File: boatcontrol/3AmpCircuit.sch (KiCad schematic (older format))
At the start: 5 parts, among them K901 G5RL-K1A-E-DC12, Q901 T9-818 3A, SW901 ESB30, SW902 ESB30

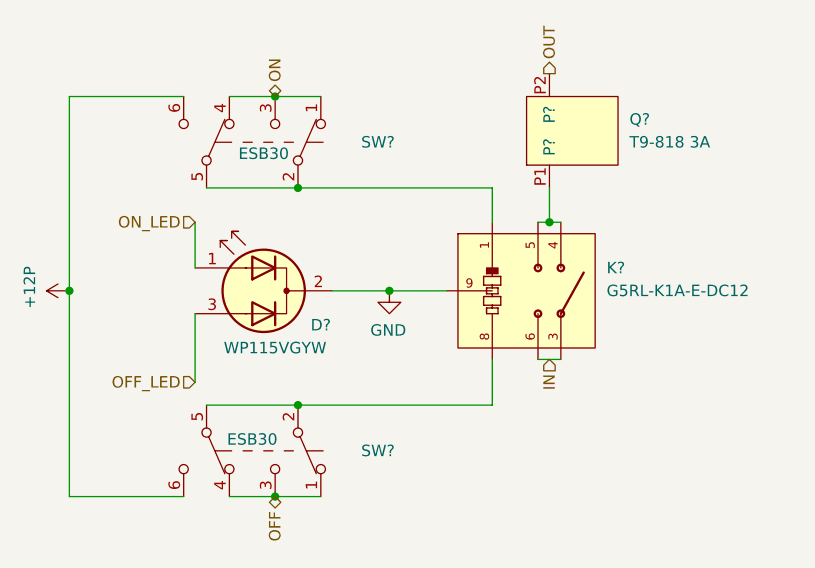
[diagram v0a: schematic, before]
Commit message: Change inductors
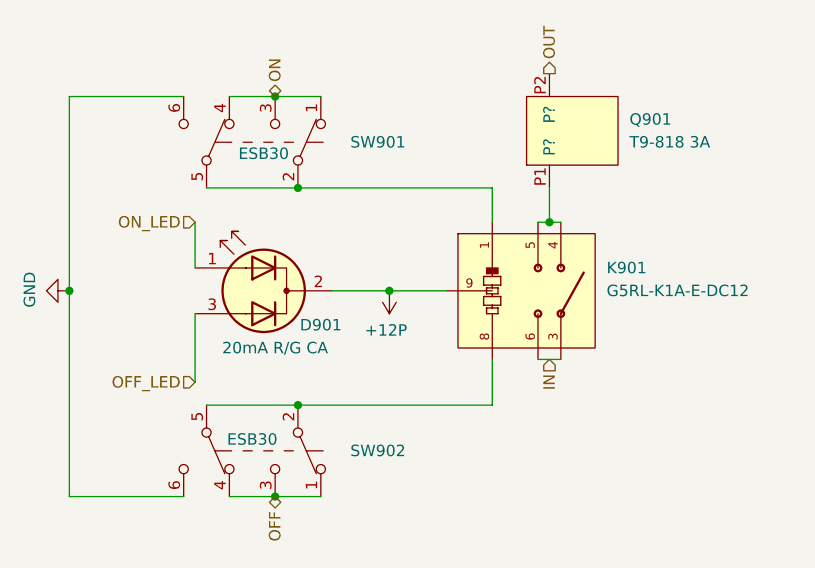
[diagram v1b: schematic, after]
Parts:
- D901: value WP115VGYW -> 20mA R/G CA; Manufacturer (none) -> Kingbright; Model (none) -> WP59EGW/CA
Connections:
- net +12P: now also D901.2 (K), K901.9 (C9); no longer SW901.6 (C), SW902.6 (C)
- net GND: now also SW901.6 (C), SW902.6 (C); no longer D901.2 (K), K901.9 (C9)
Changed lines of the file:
@@
 $Descr A4 11693 8268
 encoding utf-8
-Sheet 12 87
+Sheet 11 87
 Title "Boat Control Hat"
 Date "2020-07-09"
@@
 AR Path="/D1BB8DB4/5F75E923/60474907/6283485A" Ref="Q?"  Part="1"
 AR Path="/D1BB8DB4/5F75E923/60474911/6283485A" Ref="Q?"  Part="1"
-F 0 "Q?" V 7200 2750 50  0000 R CNN
+F 0 "Q901" V 7200 2750 50  0000 R CNN
 F 1 "T9-818 3A" V 7100 2750 50  0000 R CNN
 F 2 "BoatControl:Schurter_Circuit_Breaker" H 7150 3300 50  0001 C CNN
@@
 AR Path="/D1BB8DB4/5F75E923/60474907/63E25899" Ref="SW?"  Part="1"
 AR Path="/D1BB8DB4/5F75E923/60474911/63E25899" Ref="SW?"  Part="1"
-F 0 "SW?" V 6050 3900 50  0000 C CNN
+F 0 "SW901" V 6050 3900 50  0000 C CNN
 F 1 " ESB30" V 6000 3400 50  0000 C CNN
 F 2 "BoatControl:SW_PUSH_ESB30_DPDT" H 6050 3550 50  0001 C CNN
@@
 L power:GND #PWR?
 U 1 1 63ED7D79
-P 6650 4000
+P 5250 4000
 AR Path="/5FBFBEC9/63ED7D79" Ref="#PWR?"  Part="1"
 AR Path="/768425E1/63ED7D79" Ref="#PWR?"  Part="1"
@@
 AR Path="/D1BB8DB4/5F75E923/60474907/63ED7D79" Ref="#PWR?"  Part="1"
 AR Path="/D1BB8DB4/5F75E923/60474911/63ED7D79" Ref="#PWR?"  Part="1"
-F 0 "#PWR?" H 6650 3750 50  0001 C CNN
-F 1 "GND" H 6655 3827 50  0000 C CNN
-F 2 "" H 6650 4000 50  0001 C CNN
-F 3 "" H 6650 4000 50  0001 C CNN
-	1    6650 4000
-	-1   0    0    -1
+F 0 "#PWR0902" H 5250 3750 50  0001 C CNN
+F 1 "GND" H 5255 3827 50  0000 C CNN
+F 2 "" H 5250 4000 50  0001 C CNN
+F 3 "" H 5250 4000 50  0001 C CNN
+	1    5250 4000
+	0    1    -1   0
 $EndComp
 $Comp
 L power:+12P #PWR?
 U 1 1 D2B5CDA0
-P 5250 4000
+P 6650 4000
 AR Path="/5FBFBEC9/D2B5CDA0" Ref="#PWR?"  Part="1"
 AR Path="/768425E1/D2B5CDA0" Ref="#PWR?"  Part="1"
@@
 AR Path="/D1BB8DB4/5F75E923/60474907/D2B5CDA0" Ref="#PWR?"  Part="1"
 AR Path="/D1BB8DB4/5F75E923/60474911/D2B5CDA0" Ref="#PWR?"  Part="1"
-F 0 "#PWR?" H 5250 3850 50  0001 C CNN
-F 1 "+12P" H 5265 4173 50  0000 C CNN
-F 2 "" H 5250 4000 50  0001 C CNN
-F 3 "" H 5250 4000 50  0001 C CNN
-	1    5250 4000
-	0    -1   -1   0
+F 0 "#PWR0901" H 6650 3850 50  0001 C CNN
+F 1 "+12P" H 6665 4173 50  0000 C CNN
+F 2 "" H 6650 4000 50  0001 C CNN
+F 3 "" H 6650 4000 50  0001 C CNN
+	1    6650 4000
+	-1   0    0    1
 $EndComp
 $Comp
@@
 AR Path="/D1BB8DB4/5F75E923/60474907/D2B5CD9C" Ref="SW?"  Part="1"
 AR Path="/D1BB8DB4/5F75E923/60474911/D2B5CD9C" Ref="SW?"  Part="1"
-F 0 "SW?" V 6050 5250 50  0000 C CNN
+F 0 "SW902" V 6050 5250 50  0000 C CNN
 F 1 " ESB30" V 6000 4700 50  0000 C CNN
 F 2 "BoatControl:SW_PUSH_ESB30_DPDT" H 6050 4900 50  0001 C CNN
@@
 AR Path="/D1BB8DB4/5F75E923/60474907/E14E2027" Ref="D?"  Part="1"
 AR Path="/D1BB8DB4/5F75E923/60474911/E14E2027" Ref="D?"  Part="1"
-F 0 "D?" H 5850 3850 50  0000 C CNN
-F 1 "WP115VGYW" H 6050 3750 50  0000 C CNN
+F 0 "D901" H 5850 3850 50  0000 C CNN
+F 1 "20mA R/G CA" H 6050 3750 50  0000 C CNN
 F 2 "LED_THT:LED_D5.0mm-3" H 6100 4000 50  0001 C CNN
-F 3 "https://www.mouser.ca/datasheet/2/216/WP115VGYW-232005.pdf" H 6100 4000 50  0001 C CNN
+F 3 "http://www.kingbrightusa.com/images/catalog/SPEC/WP59EGW-CA.pdf" H 6100 4000 50  0001 C CNN
+F 4 "WP59EGW/CA" H 6100 4000 50  0001 C CNN "Model"
+F 5 "Kingbright" H 6100 4000 50  0001 C CNN "Manufacturer"
 	1    6100 4000
 	-1   0    0    -1
@@
 AR Path="/D1BB8DB4/5F75E923/60474907/D2F4D9A8" Ref="K?"  Part="1"
 AR Path="/D1BB8DB4/5F75E923/60474911/D2F4D9A8" Ref="K?"  Part="1"
-F 0 "K?" H 7600 4100 50  0000 L CNN
+F 0 "K901" H 7600 4100 50  0000 L CNN
 F 1 "G5RL-K1A-E-DC12" H 7600 4000 50  0000 L CNN
 F 2 "RELAY_G5RL-K1A-E-DC12" H 7600 4150 50  0001 L BNN

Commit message: CRC ErrorFree
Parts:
- renumbered D901 to D1101, K901 to K1101, Q901 to Q1101, SW901 to SW1101, SW902 to SW1102

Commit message: Resistance is futile
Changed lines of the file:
@@
 $Descr A4 11693 8268
 encoding utf-8
-Sheet 36 87
+Sheet 11 87
 Title "Boat Control Hat"
 Date "2020-07-09"
@@
 AR Path="/D1BB8DB4/5F75E923/60474907/6283485A" Ref="Q?"  Part="1"
 AR Path="/D1BB8DB4/5F75E923/60474911/6283485A" Ref="Q?"  Part="1"
-F 0 "Q3801" V 7200 2750 50  0000 R CNN
+F 0 "Q1101" V 7200 2750 50  0000 R CNN
 F 1 "T9-818 3A" V 7100 2750 50  0000 R CNN
 F 2 "BoatControl:Schurter_Circuit_Breaker" H 7150 3300 50  0001 C CNN
@@
 AR Path="/D1BB8DB4/5F75E923/60474907/63E25899" Ref="SW?"  Part="1"
 AR Path="/D1BB8DB4/5F75E923/60474911/63E25899" Ref="SW?"  Part="1"
-F 0 "SW3801" V 6050 3900 50  0000 C CNN
+F 0 "SW1101" V 6050 3900 50  0000 C CNN
 F 1 " ESB30" V 6000 3400 50  0000 C CNN
 F 2 "BoatControl:SW_PUSH_ESB30_DPDT" H 6050 3550 50  0001 C CNN
@@
 AR Path="/D1BB8DB4/5F75E923/60474907/D2B5CD9C" Ref="SW?"  Part="1"
 AR Path="/D1BB8DB4/5F75E923/60474911/D2B5CD9C" Ref="SW?"  Part="1"
-F 0 "SW3802" V 6050 5250 50  0000 C CNN
+F 0 "SW1102" V 6050 5250 50  0000 C CNN
 F 1 " ESB30" V 6000 4700 50  0000 C CNN
 F 2 "BoatControl:SW_PUSH_ESB30_DPDT" H 6050 4900 50  0001 C CNN
@@
 AR Path="/D1BB8DB4/5F75E923/60474907/E14E2027" Ref="D?"  Part="1"
 AR Path="/D1BB8DB4/5F75E923/60474911/E14E2027" Ref="D?"  Part="1"
-F 0 "D3801" H 5850 3850 50  0000 C CNN
+F 0 "D1101" H 5850 3850 50  0000 C CNN
 F 1 "20mA R/G CA" H 6050 3750 50  0000 C CNN
 F 2 "LED_THT:LED_D5.0mm-3" H 6100 4000 50  0001 C CNN
@@
 AR Path="/D1BB8DB4/5F75E923/60474907/D2F4D9A8" Ref="K?"  Part="1"
 AR Path="/D1BB8DB4/5F75E923/60474911/D2F4D9A8" Ref="K?"  Part="1"
-F 0 "K3801" H 7600 4100 50  0000 L CNN
+F 0 "K1101" H 7600 4100 50  0000 L CNN
 F 1 "G5RL-K1A-E-DC12" H 7600 4000 50  0000 L CNN
 F 2 "RELAY_G5RL-K1A-E-DC12" H 7600 4150 50  0001 L BNN

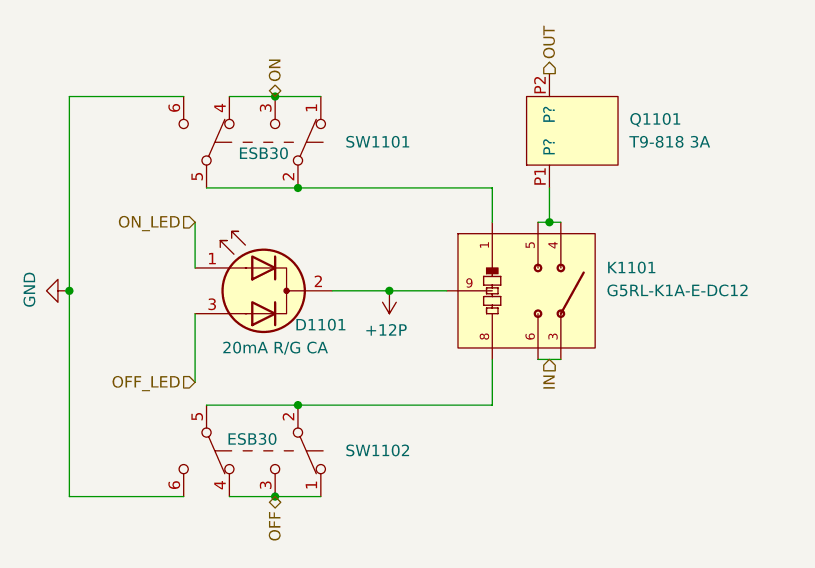
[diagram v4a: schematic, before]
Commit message: Remove resistor on protection, change MOSFET
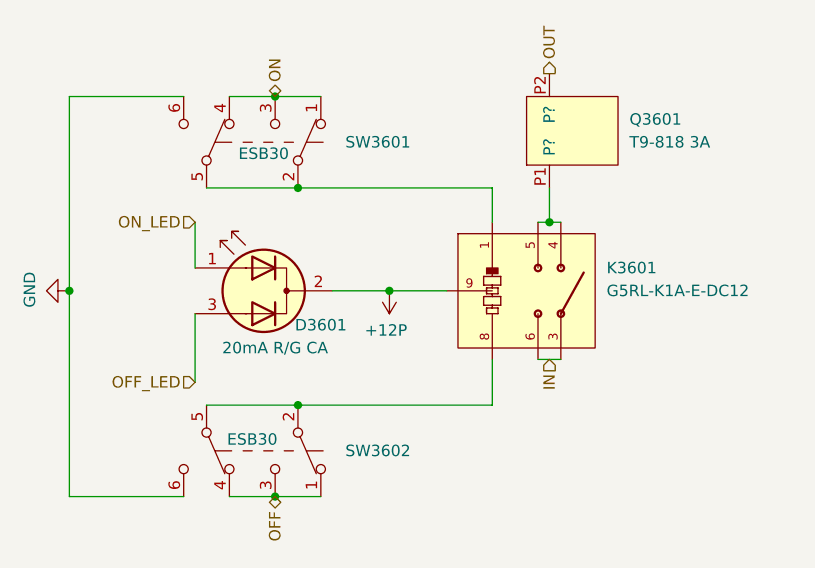
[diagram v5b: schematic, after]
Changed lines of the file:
@@
 $Descr A4 11693 8268
 encoding utf-8
-Sheet 11 87
+Sheet 36 87
 Title "Boat Control Hat"
 Date "2020-07-09"
@@
 AR Path="/D1BB8DB4/5F75E923/60474907/6283485A" Ref="Q?"  Part="1"
 AR Path="/D1BB8DB4/5F75E923/60474911/6283485A" Ref="Q?"  Part="1"
-F 0 "Q1101" V 7200 2750 50  0000 R CNN
+F 0 "Q3601" V 7200 2750 50  0000 R CNN
 F 1 "T9-818 3A" V 7100 2750 50  0000 R CNN
 F 2 "BoatControl:Schurter_Circuit_Breaker" H 7150 3300 50  0001 C CNN
@@
 AR Path="/D1BB8DB4/5F75E923/60474907/63E25899" Ref="SW?"  Part="1"
 AR Path="/D1BB8DB4/5F75E923/60474911/63E25899" Ref="SW?"  Part="1"
-F 0 "SW1101" V 6050 3900 50  0000 C CNN
+F 0 "SW3601" V 6050 3900 50  0000 C CNN
 F 1 " ESB30" V 6000 3400 50  0000 C CNN
 F 2 "BoatControl:SW_PUSH_ESB30_DPDT" H 6050 3550 50  0001 C CNN
@@
 AR Path="/D1BB8DB4/5F75E923/60474907/63ED7D79" Ref="#PWR?"  Part="1"
 AR Path="/D1BB8DB4/5F75E923/60474911/63ED7D79" Ref="#PWR?"  Part="1"
-F 0 "#PWR03801" H 5250 3750 50  0001 C CNN
+F 0 "#PWR03601" H 5250 3750 50  0001 C CNN
 F 1 "GND" H 5255 3827 50  0000 C CNN
 F 2 "" H 5250 4000 50  0001 C CNN
@@
 AR Path="/D1BB8DB4/5F75E923/60474907/D2B5CDA0" Ref="#PWR?"  Part="1"
 AR Path="/D1BB8DB4/5F75E923/60474911/D2B5CDA0" Ref="#PWR?"  Part="1"
-F 0 "#PWR03802" H 6650 3850 50  0001 C CNN
+F 0 "#PWR03602" H 6650 3850 50  0001 C CNN
 F 1 "+12P" H 6665 4173 50  0000 C CNN
 F 2 "" H 6650 4000 50  0001 C CNN
@@
 AR Path="/D1BB8DB4/5F75E923/60474907/D2B5CD9C" Ref="SW?"  Part="1"
 AR Path="/D1BB8DB4/5F75E923/60474911/D2B5CD9C" Ref="SW?"  Part="1"
-F 0 "SW1102" V 6050 5250 50  0000 C CNN
+F 0 "SW3602" V 6050 5250 50  0000 C CNN
 F 1 " ESB30" V 6000 4700 50  0000 C CNN
 F 2 "BoatControl:SW_PUSH_ESB30_DPDT" H 6050 4900 50  0001 C CNN
@@
 AR Path="/D1BB8DB4/5F75E923/60474907/E14E2027" Ref="D?"  Part="1"
 AR Path="/D1BB8DB4/5F75E923/60474911/E14E2027" Ref="D?"  Part="1"
-F 0 "D1101" H 5850 3850 50  0000 C CNN
+F 0 "D3601" H 5850 3850 50  0000 C CNN
 F 1 "20mA R/G CA" H 6050 3750 50  0000 C CNN
 F 2 "LED_THT:LED_D5.0mm-3" H 6100 4000 50  0001 C CNN
@@
 AR Path="/D1BB8DB4/5F75E923/60474907/D2F4D9A8" Ref="K?"  Part="1"
 AR Path="/D1BB8DB4/5F75E923/60474911/D2F4D9A8" Ref="K?"  Part="1"
-F 0 "K1101" H 7600 4100 50  0000 L CNN
+F 0 "K3601" H 7600 4100 50  0000 L CNN
 F 1 "G5RL-K1A-E-DC12" H 7600 4000 50  0000 L CNN
 F 2 "RELAY_G5RL-K1A-E-DC12" H 7600 4150 50  0001 L BNN

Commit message: Try labels on subcharts
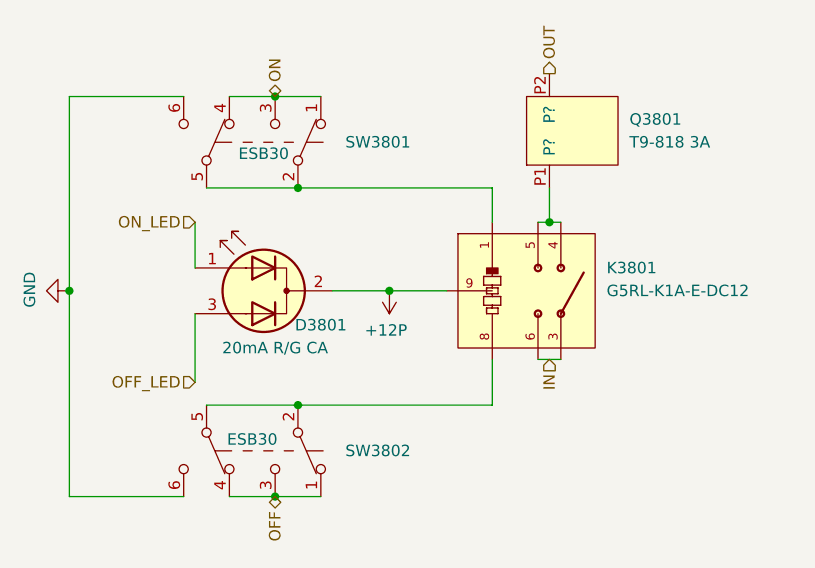
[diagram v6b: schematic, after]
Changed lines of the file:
@@
 AR Path="/D1BB8DB4/5F75E923/60474907/6283485A" Ref="Q?"  Part="1"
 AR Path="/D1BB8DB4/5F75E923/60474911/6283485A" Ref="Q?"  Part="1"
-F 0 "Q3601" V 7200 2750 50  0000 R CNN
+F 0 "Q3801" V 7200 2750 50  0000 R CNN
 F 1 "T9-818 3A" V 7100 2750 50  0000 R CNN
 F 2 "BoatControl:Schurter_Circuit_Breaker" H 7150 3300 50  0001 C CNN
@@
 AR Path="/D1BB8DB4/5F75E923/60474907/63E25899" Ref="SW?"  Part="1"
 AR Path="/D1BB8DB4/5F75E923/60474911/63E25899" Ref="SW?"  Part="1"
-F 0 "SW3601" V 6050 3900 50  0000 C CNN
+F 0 "SW3801" V 6050 3900 50  0000 C CNN
 F 1 " ESB30" V 6000 3400 50  0000 C CNN
 F 2 "BoatControl:SW_PUSH_ESB30_DPDT" H 6050 3550 50  0001 C CNN
@@
 AR Path="/D1BB8DB4/5F75E923/60474907/63ED7D79" Ref="#PWR?"  Part="1"
 AR Path="/D1BB8DB4/5F75E923/60474911/63ED7D79" Ref="#PWR?"  Part="1"
-F 0 "#PWR03601" H 5250 3750 50  0001 C CNN
+F 0 "#PWR03801" H 5250 3750 50  0001 C CNN
 F 1 "GND" H 5255 3827 50  0000 C CNN
 F 2 "" H 5250 4000 50  0001 C CNN
@@
 AR Path="/D1BB8DB4/5F75E923/60474907/D2B5CDA0" Ref="#PWR?"  Part="1"
 AR Path="/D1BB8DB4/5F75E923/60474911/D2B5CDA0" Ref="#PWR?"  Part="1"
-F 0 "#PWR03602" H 6650 3850 50  0001 C CNN
+F 0 "#PWR03802" H 6650 3850 50  0001 C CNN
 F 1 "+12P" H 6665 4173 50  0000 C CNN
 F 2 "" H 6650 4000 50  0001 C CNN
@@
 AR Path="/D1BB8DB4/5F75E923/60474907/D2B5CD9C" Ref="SW?"  Part="1"
 AR Path="/D1BB8DB4/5F75E923/60474911/D2B5CD9C" Ref="SW?"  Part="1"
-F 0 "SW3602" V 6050 5250 50  0000 C CNN
+F 0 "SW3802" V 6050 5250 50  0000 C CNN
 F 1 " ESB30" V 6000 4700 50  0000 C CNN
 F 2 "BoatControl:SW_PUSH_ESB30_DPDT" H 6050 4900 50  0001 C CNN
@@
 AR Path="/D1BB8DB4/5F75E923/60474907/E14E2027" Ref="D?"  Part="1"
 AR Path="/D1BB8DB4/5F75E923/60474911/E14E2027" Ref="D?"  Part="1"
-F 0 "D3601" H 5850 3850 50  0000 C CNN
+F 0 "D3801" H 5850 3850 50  0000 C CNN
 F 1 "20mA R/G CA" H 6050 3750 50  0000 C CNN
 F 2 "LED_THT:LED_D5.0mm-3" H 6100 4000 50  0001 C CNN
@@
 AR Path="/D1BB8DB4/5F75E923/60474907/D2F4D9A8" Ref="K?"  Part="1"
 AR Path="/D1BB8DB4/5F75E923/60474911/D2F4D9A8" Ref="K?"  Part="1"
-F 0 "K3601" H 7600 4100 50  0000 L CNN
+F 0 "K3801" H 7600 4100 50  0000 L CNN
 F 1 "G5RL-K1A-E-DC12" H 7600 4000 50  0000 L CNN
 F 2 "RELAY_G5RL-K1A-E-DC12" H 7600 4150 50  0001 L BNN

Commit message: Fix graphics
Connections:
- net TO_FUSE: now reaches K1101.4 (NO), K1101.5 (NO), Q1101.P1 (P?)
- net ON_COIL: now reaches K1101.1 (C1), SW1101.2 (B), SW1101.5 (B)
- net OFF_COIL: now reaches K1101.8 (C8), SW1102.2 (B), SW1102.5 (B)
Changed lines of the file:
@@
 $Descr A4 11693 8268
 encoding utf-8
-Sheet 36 87
+Sheet 26 87
 Title "Boat Control Hat"
 Date "2020-07-09"
@@
 	1    0    0    -1
 $EndComp
+Text Label 6750 3550 0    50   ~ 0
+ON_COIL
+Text Label 6750 4500 0    50   ~ 0
+OFF_COIL
+Text Label 7350 3650 0    50   ~ 0
+TO_FUSE
 $EndSCHEMATC

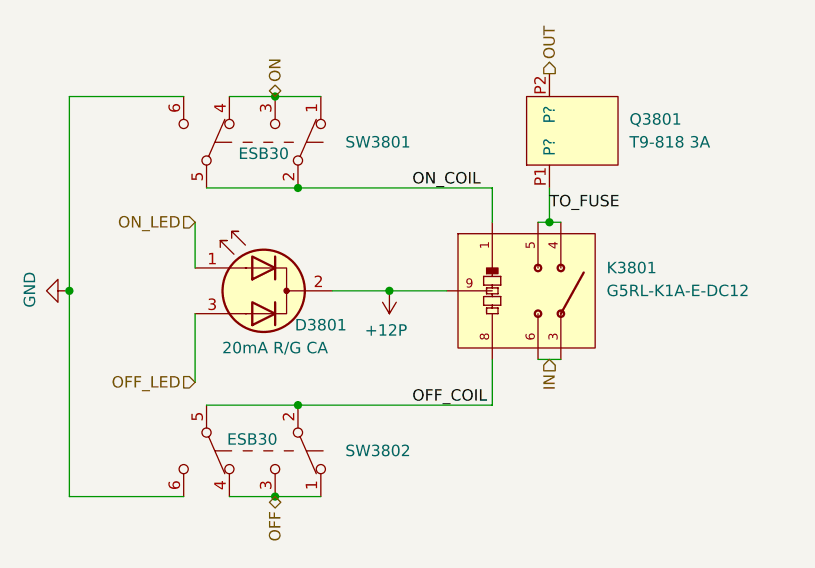
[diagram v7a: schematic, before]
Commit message: Make 12V PSU Optional
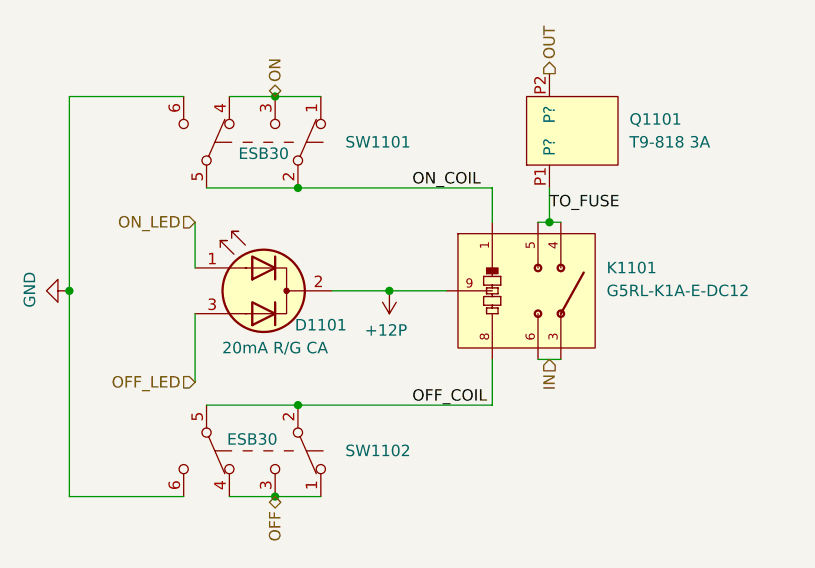
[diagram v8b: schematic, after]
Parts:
- K1101: Manufacturer (none) -> Omron
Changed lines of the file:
@@
 $Descr A4 11693 8268
 encoding utf-8
-Sheet 26 87
+Sheet 11 87
 Title "Boat Control Hat"
 Date "2020-07-09"
@@
 AR Path="/D1BB8DB4/5F75E923/60474907/6283485A" Ref="Q?"  Part="1"
 AR Path="/D1BB8DB4/5F75E923/60474911/6283485A" Ref="Q?"  Part="1"
-F 0 "Q3801" V 7200 2750 50  0000 R CNN
+F 0 "Q1101" V 7200 2750 50  0000 R CNN
 F 1 "T9-818 3A" V 7100 2750 50  0000 R CNN
 F 2 "BoatControl:Schurter_Circuit_Breaker" H 7150 3300 50  0001 C CNN
@@
 AR Path="/D1BB8DB4/5F75E923/60474907/63E25899" Ref="SW?"  Part="1"
 AR Path="/D1BB8DB4/5F75E923/60474911/63E25899" Ref="SW?"  Part="1"
-F 0 "SW3801" V 6050 3900 50  0000 C CNN
+F 0 "SW1101" V 6050 3900 50  0000 C CNN
 F 1 " ESB30" V 6000 3400 50  0000 C CNN
 F 2 "BoatControl:SW_PUSH_ESB30_DPDT" H 6050 3550 50  0001 C CNN
@@
 AR Path="/D1BB8DB4/5F75E923/60474907/63ED7D79" Ref="#PWR?"  Part="1"
 AR Path="/D1BB8DB4/5F75E923/60474911/63ED7D79" Ref="#PWR?"  Part="1"
-F 0 "#PWR03801" H 5250 3750 50  0001 C CNN
+F 0 "#PWR01101" H 5250 3750 50  0001 C CNN
 F 1 "GND" H 5255 3827 50  0000 C CNN
 F 2 "" H 5250 4000 50  0001 C CNN
@@
 AR Path="/D1BB8DB4/5F75E923/60474907/D2B5CDA0" Ref="#PWR?"  Part="1"
 AR Path="/D1BB8DB4/5F75E923/60474911/D2B5CDA0" Ref="#PWR?"  Part="1"
-F 0 "#PWR03802" H 6650 3850 50  0001 C CNN
+F 0 "#PWR01102" H 6650 3850 50  0001 C CNN
 F 1 "+12P" H 6665 4173 50  0000 C CNN
 F 2 "" H 6650 4000 50  0001 C CNN
@@
 AR Path="/D1BB8DB4/5F75E923/60474907/D2B5CD9C" Ref="SW?"  Part="1"
 AR Path="/D1BB8DB4/5F75E923/60474911/D2B5CD9C" Ref="SW?"  Part="1"
-F 0 "SW3802" V 6050 5250 50  0000 C CNN
+F 0 "SW1102" V 6050 5250 50  0000 C CNN
 F 1 " ESB30" V 6000 4700 50  0000 C CNN
 F 2 "BoatControl:SW_PUSH_ESB30_DPDT" H 6050 4900 50  0001 C CNN
@@
 AR Path="/D1BB8DB4/5F75E923/60474907/E14E2027" Ref="D?"  Part="1"
 AR Path="/D1BB8DB4/5F75E923/60474911/E14E2027" Ref="D?"  Part="1"
-F 0 "D3801" H 5850 3850 50  0000 C CNN
+F 0 "D1101" H 5850 3850 50  0000 C CNN
 F 1 "20mA R/G CA" H 6050 3750 50  0000 C CNN
 F 2 "LED_THT:LED_D5.0mm-3" H 6100 4000 50  0001 C CNN
@@
 AR Path="/D1BB8DB4/5F75E923/60474907/D2F4D9A8" Ref="K?"  Part="1"
 AR Path="/D1BB8DB4/5F75E923/60474911/D2F4D9A8" Ref="K?"  Part="1"
-F 0 "K3801" H 7600 4100 50  0000 L CNN
+F 0 "K1101" H 7600 4100 50  0000 L CNN
 F 1 "G5RL-K1A-E-DC12" H 7600 4000 50  0000 L CNN
 F 2 "RELAY_G5RL-K1A-E-DC12" H 7600 4150 50  0001 L BNN
-F 3 "Omron" H 7600 4250 50  0001 L BNN
+F 3 "https://www.mouser.ca/datasheet/2/307/en-g5rl_uk-1061771.pdf" H 7600 4250 50  0001 L BNN
+F 4 "Omron" H 7200 4000 50  0001 C CNN "Manufacturer"
 	1    7200 4000
 	1    0    0    -1
